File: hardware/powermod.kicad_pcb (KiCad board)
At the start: 4 copper layers, 65 x 40 mm, 77 parts, among them J1 USB_C_IN, J2 USB_C_OUT, J3 JST_PH_2, J4 STEMMA_QT, J5 SWD_HDR, Q1 AON7407, Q2 AON7407, Q3 BSS138, SW1 BUTTON, U1 BM8563, U2 PY32F003F18P6, U3 TPS63020DSJR, U4 TP4056, U5 XC6206P332MR, Y1 32.768kHz

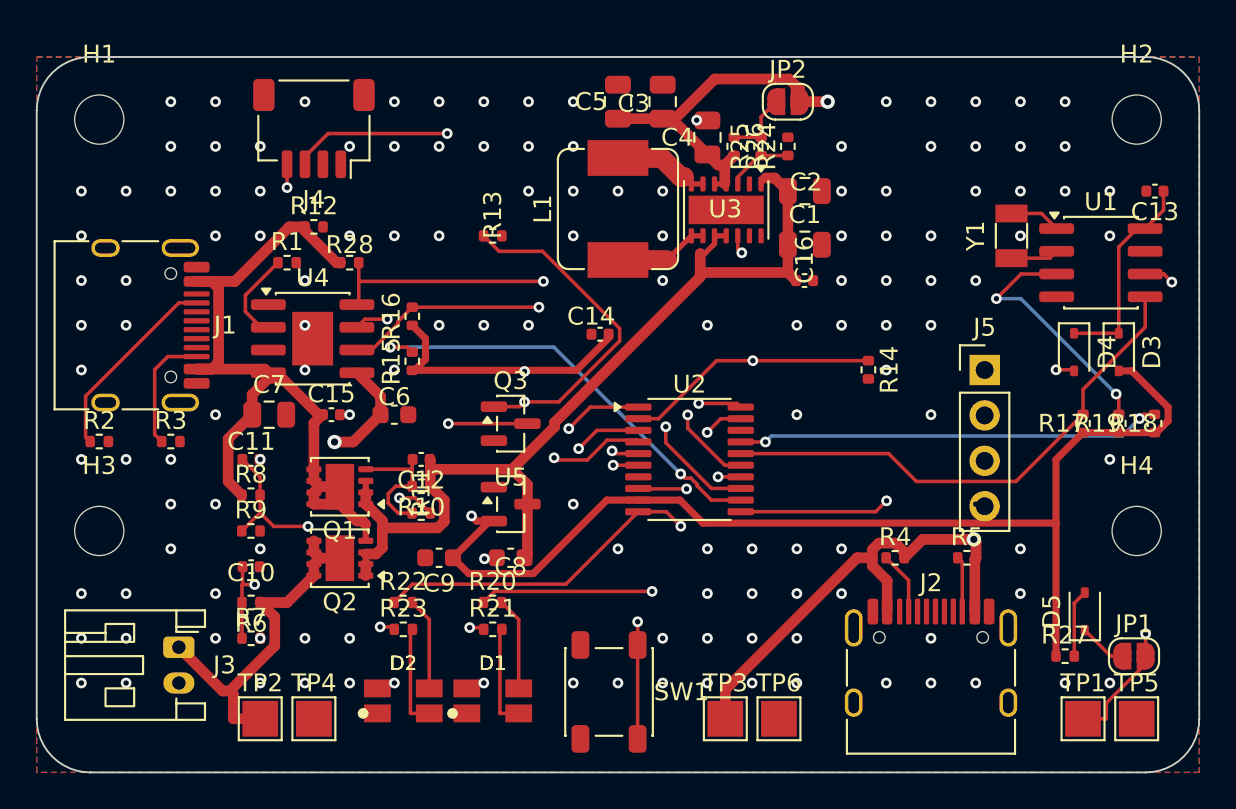
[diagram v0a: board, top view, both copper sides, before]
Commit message: hardware: full Freerouting reroute for the 4-pin SWD header (J5 1x04) [WIP]
Re-placed J5 as 1x04 (user placement) + user component tweaks, then full
strip-and-reroute (Freerouting v2.2.4 -mp 50: 121->7). finish_board: 158 GND
stitch vias + 5 island ties -> 409 tracks, 202 vias. pad-diff 226/226, DRC
clean apart from the 4 known U3 track_width necks.

Remaining for hand-finish: 7 USB-C large-pad escapes (VBUS->J1, VOUT->J2/TP3/R5)
+ 2 GND pads (C10.2, U2.7) whose pour islands are too cramped for a tie via
(need a ~1mm part nudge). U2.7 is the MCU ground - must be tied.

Co-Authored-By: Claude Opus 4.8 <noreply@anthropic.com>
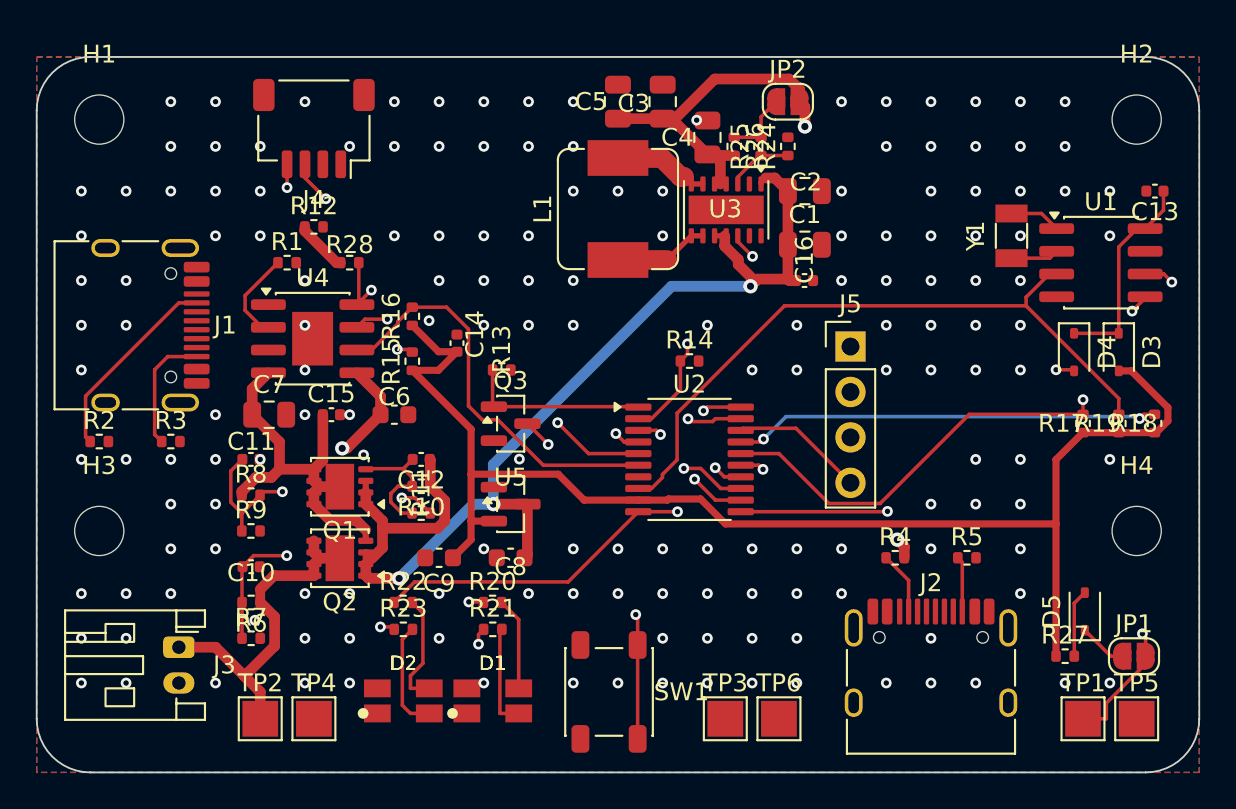
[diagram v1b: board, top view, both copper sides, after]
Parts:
- moved R14 10.0 mm to (36.5, 17.0), turned to 0 degrees
- moved C14 8.02 mm to (23.5, 16.0), turned to 90 degrees
- moved J5 7.61 mm to (45.5, 16.2)
- moved R13 7.52 mm to (26.0, 17.5)
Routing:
- net VOUT: track 77.2 -> 46.7 mm
- net VBUS: track 44.1 -> 24.8 mm
- net Q1_GATE_DRV: track 26.5 -> 10.2 mm, vias 2 -> 0
- net 3V3: track 87.8 -> 76.0 mm, vias 2 -> 0
- net SCL: track 35.4 -> 43.4 mm
- net CONV_EN: track 21.5 -> 13.6 mm
- net VSYS: track 54.5 -> 62.4 mm, vias 0 -> 3
- net LED_BAT_A: track 37.0 -> 29.4 mm
- net NRST: track 0.00 -> 7.45 mm
- net VBAT_DIV: track 29.7 -> 34.4 mm
- net CHG_CHRG: track 28.1 -> 31.4 mm
- net LED_PWR_A: track 22.1 -> 20.4 mm
- net CHG_CE: track 25.3 -> 23.9 mm
- net Q3_DRAIN: track 11.8 -> 13.0 mm
- net D2_RED: track 5.19 -> 6.39 mm
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
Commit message: hardware: full reroute after placement loosening; both GND pads tied
User spread C10/U2/J5. Full Freerouting reroute (121->6). finish_board tied
C10.2 GND cleanly this time; U2.7 (MCU GND) tied via a 0.9mm F.Cu stub+via
(the pour island was still too tight for a direct plane via). 387 tracks,
195 vias. pad-diff 226/226, DRC clean except 4 known necks. Power trunks 0.6mm,
switch node 1.1mm. Remaining: 5 USB-C large-pad escapes to hand-route.

Co-Authored-By: Claude Opus 4.8 <noreply@anthropic.com>
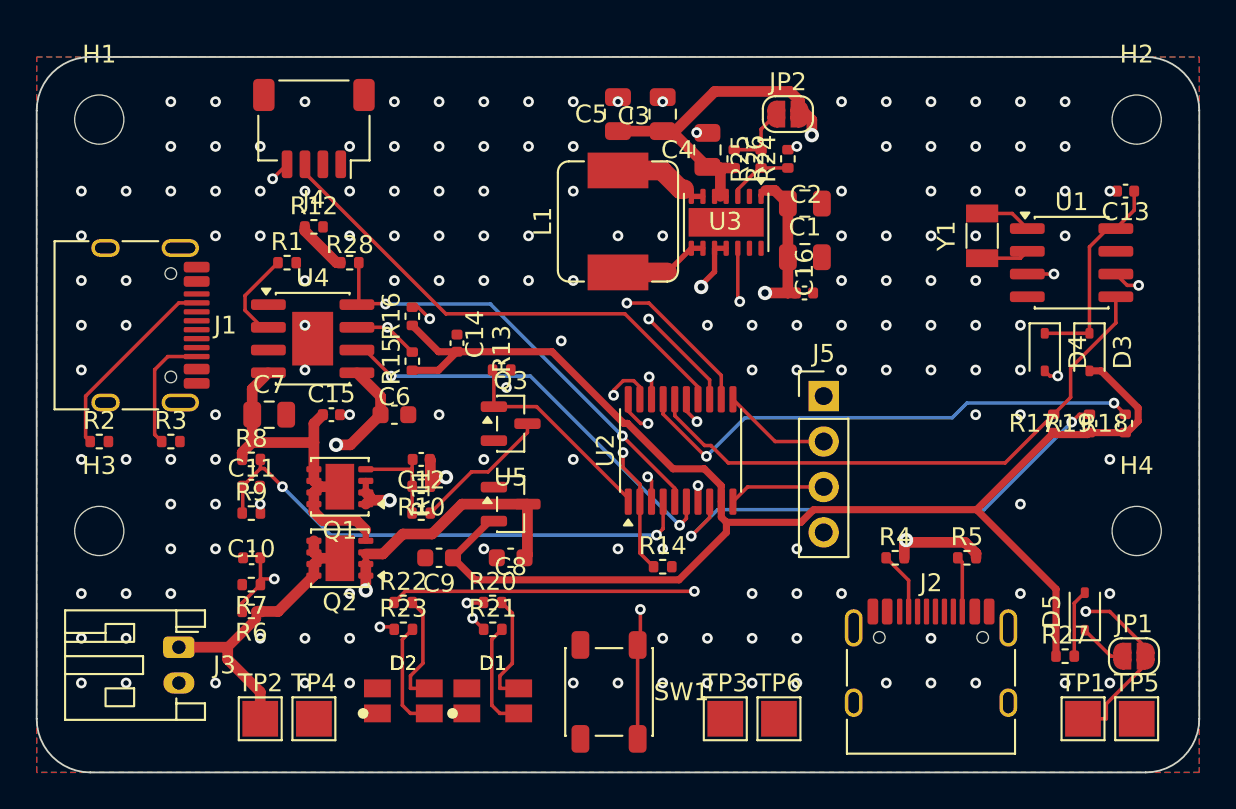
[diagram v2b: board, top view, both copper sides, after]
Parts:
- moved R14 11.6 mm to (35.0, 28.5)
- moved J5 3.15 mm to (44.0, 19.0)
- moved R7 3.00 mm to (12.0, 29.5), turned to 180 degrees
- moved R8 2.00 mm to (12.0, 22.5)
- moved C13 1.64 mm to (60.9, 7.50)
- moved D3 1.64 mm to (58.9, 16.5)
- moved D4 1.64 mm to (56.4, 16.5)
- moved R17 1.64 mm to (56.9, 20.5)
- moved R18 1.64 mm to (60.9, 20.5)
- moved R19 1.64 mm to (58.9, 20.5)
- moved U1 1.64 mm to (57.9, 11.5)
- moved Y1 1.64 mm to (52.9, 10.0)
- moved C11 1.50 mm to (12.0, 24.0)
- moved R9 1.00 mm to (12.0, 25.5)
- moved U2 0.71 mm to (36.0, 22.0), turned to 90 degrees
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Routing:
- net LED_BAT_B: track 52.1 -> 36.5 mm, vias 2 -> 1
- net NRST: track 7.45 -> 19.6 mm, vias 0 -> 1
- net SCL: track 43.4 -> 31.6 mm
- net 3V3: track 76.0 -> 86.5 mm
- net CONV_EN: track 13.6 -> 22.3 mm
- net CHG_STDBY: track 23.0 -> 31.3 mm, vias 0 -> 3
- net SDA: track 34.7 -> 28.1 mm, vias 2 -> 0
- net CHG_CHRG: track 31.4 -> 26.0 mm, vias 3 -> 2
- net Q3_DRAIN: track 13.0 -> 7.79 mm, vias 2 -> 0
- net LED_PWR_B: track 23.7 -> 19.5 mm
- net VOUT: track 46.7 -> 50.6 mm
- net RTC_SCL: track 33.9 -> 37.8 mm
- net BUTTON: track 22.1 -> 25.5 mm
- net VBAT_DIV: track 34.4 -> 31.3 mm
- net LED_BAT_A: track 29.4 -> 32.1 mm
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
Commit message: hardware: reroute after U1-near-U2 placement; RTC bus ~34mm shorter
User moved U1 (RTC) adjacent to U2 (MCU) and J5 to the edge. Full Freerouting
reroute (121->6). All 4 GND islands now tie automatically - no stub+via hack
for U2.7 this time. 409 tracks, 198 vias, pad-diff 226/226, DRC clean except
the 4 known necks.

RTC bus shortened: RTC_INT -13.4mm, RTC_SCL -12.2mm, RTC_SDA -8.1mm, 3V3 -4.1mm.
Minor +3mm on SDA/SCL/VBUS_DIV (slow signals). Crystal still ~3mm, power trunks
0.6mm unchanged. Remaining: USB-C large-pad escapes to hand-route.

Co-Authored-By: Claude Opus 4.8 <noreply@anthropic.com>
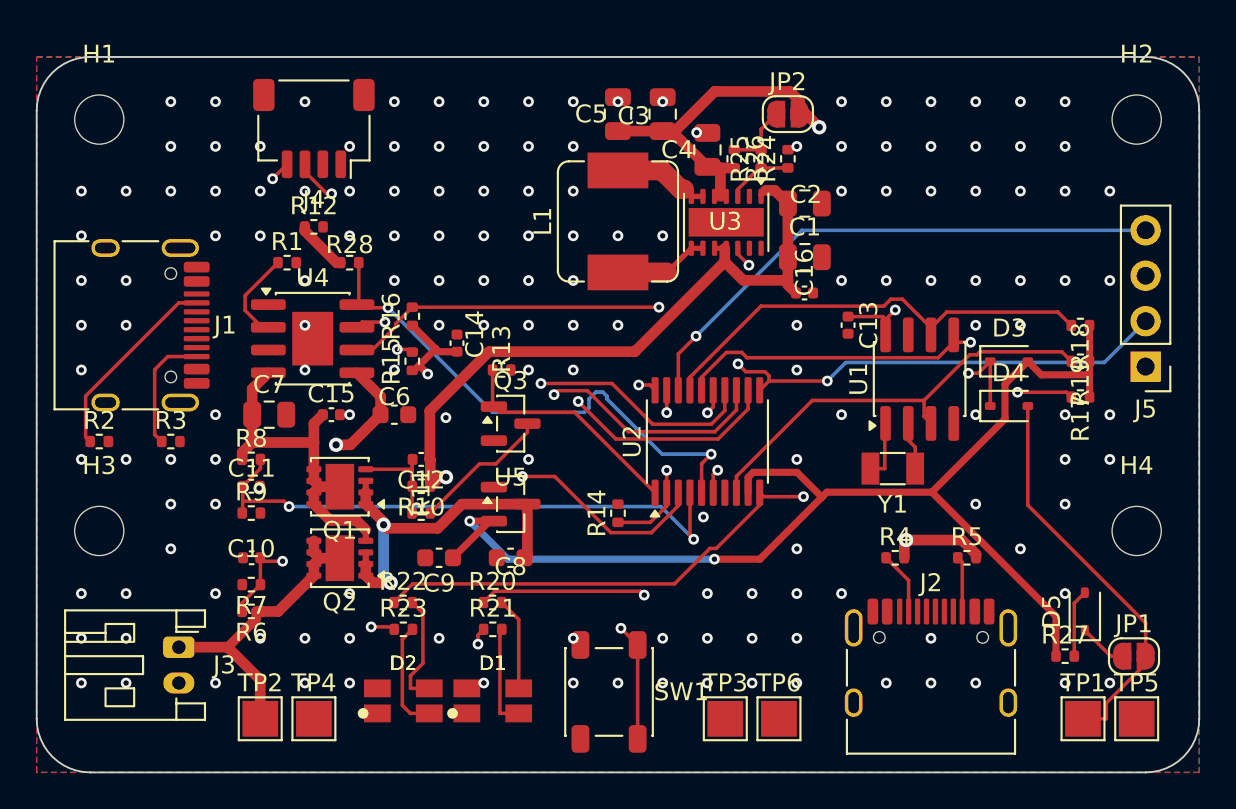
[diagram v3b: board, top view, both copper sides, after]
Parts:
- moved J5 18.1 mm to (62.0, 17.3), turned to 180 degrees
- moved C13 17.2 mm to (45.4, 15.0), turned to -90 degrees
- moved Y1 13.9 mm to (47.9, 23.0), turned to 180 degrees
- moved U1 10.7 mm to (49.4, 18.0), turned to 90 degrees
- moved R18 6.02 mm to (58.4, 15.0), turned to 180 degrees
- moved D3 4.52 mm to (54.4, 17.0), turned to 0 degrees
- moved R14 3.90 mm to (32.5, 25.5), turned to 90 degrees
- moved D4 3.61 mm to (54.4, 19.5), turned to 0 degrees
- moved R19 3.51 mm to (58.4, 17.0), turned to 180 degrees
- moved R17 2.10 mm to (58.4, 19.0), turned to 180 degrees
- moved U2 1.58 mm to (37.5, 21.5)
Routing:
- net LED_BAT_A: track 32.1 -> 54.2 mm
- net LED_BAT_B: track 36.5 -> 54.0 mm, vias 1 -> 3
- net RTC_INT: track 37.6 -> 24.2 mm, vias 3 -> 0
- net RTC_SCL: track 37.8 -> 25.6 mm, vias 3 -> 0
- net NRST: track 19.6 -> 31.0 mm
- net RTC_SDA: track 32.3 -> 24.2 mm, vias 0 -> 2
- net CHG_STDBY: track 31.3 -> 39.1 mm, vias 3 -> 2
- net LED_PWR_B: track 19.5 -> 26.1 mm
- net CHG_CE: track 25.1 -> 29.3 mm
- net 3V3: track 86.5 -> 82.4 mm, vias 0 -> 3
- net BUTTON: track 25.5 -> 21.6 mm
- net SCL: track 31.6 -> 34.7 mm
- net SDA: track 28.1 -> 31.2 mm, vias 0 -> 2
- net VBUS_DIV: track 29.1 -> 32.2 mm
- net VBACKUP: track 25.0 -> 22.4 mm, vias 2 -> 0
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
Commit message: hardware: switch-node reroute (L1N/L2) -> 0 DRC errors
User rerouted L1N/L2 uniformly at 1.1mm (single-layer F.Cu, no vias, ~9.7mm each)
right up to U3's QFN L-pins, eliminating the 4 intrinsic track_width necks that
the board carried since the ATtiny days. Error-level DRC now 0 (was 4). Only
cosmetic silk warnings remain. pad-diff 226/226, 0 unrouted. Gerbers refreshed.

Co-Authored-By: Claude Opus 4.8 <noreply@anthropic.com>
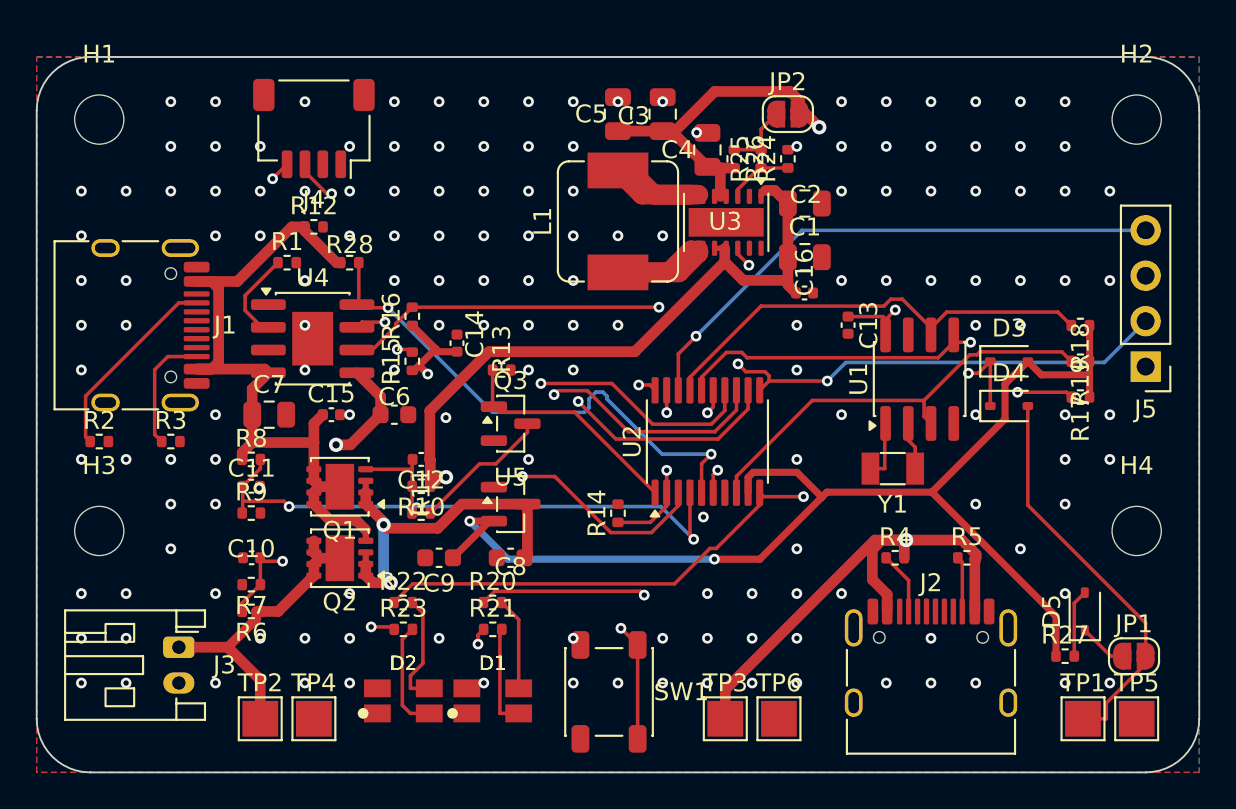
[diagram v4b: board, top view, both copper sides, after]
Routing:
- net VOUT: track 51.0 -> 75.1 mm
- net VBUS: track 22.6 -> 40.9 mm
- net L1N: track 5.31 -> 9.72 mm
- net L2: track 5.35 -> 9.72 mm
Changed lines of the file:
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@@
 	)
 	(segment
+		(start 8.945 12.55)
+		(end 9.785252 12.55)
+		(width 0.6)
+		(layer "F.Cu")
+		(net "VBUS")
+	)
+	(segment
+		(start 9.785252 12.55)
+		(end 10.17 12.934748)
+		(width 0.6)
+		(layer "F.Cu")
+		(net "VBUS")
+	)
+	(segment
+		(start 11.218232 12.55)
+		(end 14.268232 9.5)
+		(width 0.6)
+		(layer "F.Cu")
+		(net "VBUS")
+	)
+	(segment
+		(start 8.945 17.45)
+		(end 12.75 17.45)
+		(width 0.6)
+		(layer "F.Cu")
+		(net "VBUS")
+	)
+	(segment
+		(start 8.945 12.55)
+		(end 11.218232 12.55)
+		(width 0.6)
+		(layer "F.Cu")
+		(net "VBUS")
+	)
+	(segment
 		(start 12.05 21.5555)
 		(end 11.49 22.1155)
@@
 	)
 	(segment
+		(start 12.75 17.45)
+		(end 12.955 17.655)
+		(width 0.6)
+		(layer "F.Cu")
+		(net "VBUS")
+	)
+	(segment
+		(start 14.268232 9.5)
+		(end 14.99 9.5)
+		(width 0.6)
+		(layer "F.Cu")
+		(net "VBUS")
+	)
+	(segment
 		(start 15.5 21.5555)
 		(end 15.5 20.5)
@@
 	)
 	(segment
+		(start 10.17 17.065252)
+		(end 9.785252 17.45)
+		(width 0.6)
+		(layer "F.Cu")
+		(net "VBUS")
+	)
+	(segment
 		(start 14.99 9.7233)
 		(end 14.99 9.5)
@@
 	)
 	(segment
+		(start 10.17 12.934748)
+		(end 10.17 17.065252)
+		(width 0.6)
+		(layer "F.Cu")
+		(net "VBUS")
+	)
+	(segment
 		(start 15.5 23.05)
 		(end 15.5 21.5555)
@@
 	)
 	(segment
+		(start 9.785252 17.45)
+		(end 8.945 17.45)
+		(width 0.6)
+		(layer "F.Cu")
+		(net "VBUS")
+	)
+	(segment
 		(start 16.95 24.025)
 		(end 15.825 24.025)
@@
 	)
 	(segment
+		(start 47.259332 27.0089)
+		(end 48.6093 27.0089)
+		(width 0.6)
+		(layer "F.Cu")
+		(net "VOUT")
+	)
+	(segment
 		(start 42.1183 1.9279)
 		(end 42.65 2.4596)
@@
 	)
 	(segment
+		(start 46.72 27.548232)
+		(end 47.259332 27.0089)
+		(width 0.6)
+		(layer "F.Cu")
+		(net "VOUT")
+	)
+	(segment
+		(start 46.859729 27.0089)
+		(end 48.6093 27.0089)
+		(width 0.6)
+		(layer "F.Cu")
+		(net "VOUT")
+	)
+	(segment
 		(start 37.5 6.145)
 		(end 35.6566 4.3016)
@@
 	)
 	(segment
+		(start 38.5 35.368629)
+		(end 46.859729 27.0089)
+		(width 0.6)
+		(layer "F.Cu")
+		(net "VOUT")
+	)
+	(segment
 		(start 35 4.145)
 		(end 32.5 4.145)
@@
 	)
 	(segment
+		(start 47.55 31.005)
+		(end 47.55 30.05)
+		(width 0.6)
+		(layer "F.Cu")
+		(net "VOUT")
+	)
+	(segment
 		(start 38.55 7.795)
 		(end 38.225 7.795)
@@
 	)
 	(segment
+		(start 46.72 29.22)
+		(end 46.72 27.548232)
+		(width 0.6)
+		(layer "F.Cu")
+		(net "VOUT")
+	)
+	(segment
 		(start 37.9086 1.9279)
 		(end 42.1183 1.9279)
@@
 	)
 	(segment
+		(start 47.55 30.05)
+		(end 46.72 29.22)
+		(width 0.6)
+		(layer "F.Cu")
+		(net "VOUT")
+	)
+	(segment
 		(start 35.6566 4.1799)
 		(end 37.9086 1.9279)
@@
 	)
 	(segment
+		(start 38.5 37)
+		(end 38.5 35.368629)
+		(width 0.6)
+		(layer "F.Cu")
+		(net "VOUT")
+	)
+	(segment
 		(start 42.65 2.4596)
 		(end 42.65 2.8273)
@@
 		(net "VOUT")
 	)
+	(segment
+		(start 52.45 31.005)
+		(end 52.45 28.07)
+		(width 0.6)
+		(layer "F.Cu")
+		(net "VOUT")
+	)
+	(segment
+		(start 52.45 28.07)
+		(end 52.52 28)
+		(width 0.6)
+		(layer "F.Cu")
+		(net "VOUT")
+	)
 	(via
 		(at 43.7535 3.9308)
@@
 	)
 	(segment
-		(start 32.5 6.345)
-		(end 34.9517 6.345)
+		(start 34.5 7.695)
+		(end 36.9998 7.695)
 		(width 1.1)
 		(layer "F.Cu")
@@
 	)
 	(segment
-		(start 36.0029 7.3962)
-		(end 36.2012 7.3962)
+		(start 33.85 7.695)
+		(end 36.6 7.695)
 		(width 1.1)
 		(layer "F.Cu")
@@
 	)
 	(segment
-		(start 36.2012 7.3962)
-		(end 36.6 7.795)
-		(width 0.3004)
+		(start 32.5 6.345)
+		(end 33.15 6.345)
+		(width 1.1)
 		(layer "F.Cu")
 		(net "L2")
 	)
 	(segment
-		(start 37.25 7.795)
-		(end 36.6 7.795)
-		(width 0.3004)
+		(start 33.15 6.345)
+		(end 34.5 7.695)
+		(width 1.1)
 		(layer "F.Cu")
 		(net "L2")
 	)
 	(segment
-		(start 34.9517 6.345)
-		(end 36.0029 7.3962)
+		(start 32.5 6.345)
+		(end 33.85 7.695)
 		(width 1.1)
 		(layer "F.Cu")
@@
 	)
 	(segment
-		(start 35.25 12.045)
-		(end 36.6 10.695)
-		(width 0.3004)
+		(start 32.5 12.045)
+		(end 35.35 12.045)
+		(width 1.1)
 		(layer "F.Cu")
 		(net "L1N")
 	)
 	(segment
-		(start 36.6 10.695)
-		(end 37.25 10.695)
-		(width 0.3004)
+		(start 36.9998 10.9452)
+		(end 36.9998 10.795)
+		(width 1.1)
 		(layer "F.Cu")
 		(net "L1N")
@@
 	(segment
 		(start 32.5 12.045)
-		(end 35.25 12.045)
+		(end 35.9 12.045)
+		(width 1.1)
+		(layer "F.Cu")
+		(net "L1N")
+	)
+	(segment
+		(start 35.9 12.045)
+		(end 36.9998 10.9452)
+		(width 1.1)
+		(layer "F.Cu")
+		(net "L1N")
+	)
+	(segment
+		(start 35.35 12.045)
+		(end 36.6 10.795)
 		(width 1.1)
 		(layer "F.Cu")
